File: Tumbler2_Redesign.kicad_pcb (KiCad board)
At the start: 2 copper layers, 77 x 84 mm, 4 parts

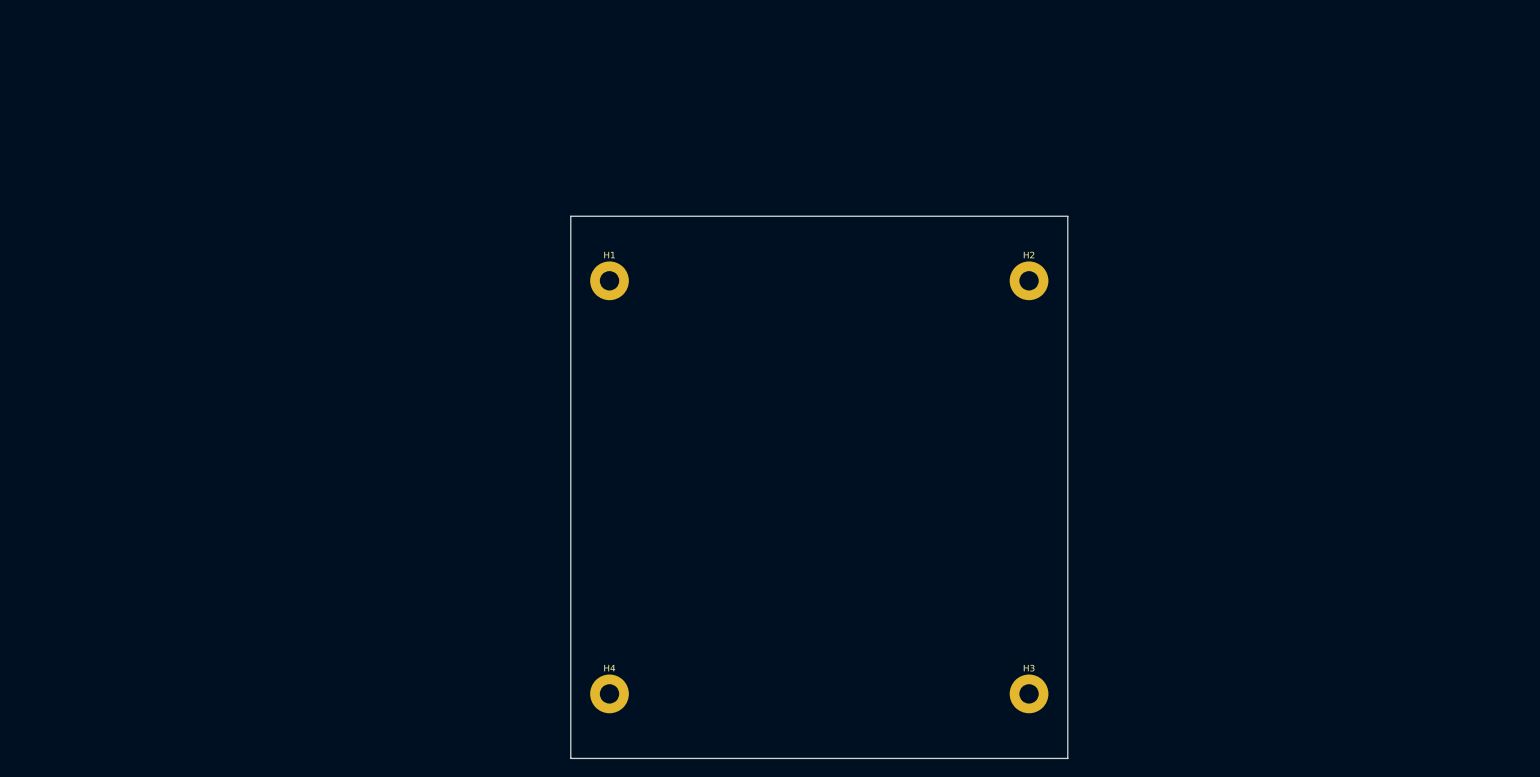
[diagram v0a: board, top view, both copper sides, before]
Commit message: Add HC-SR04 3D model
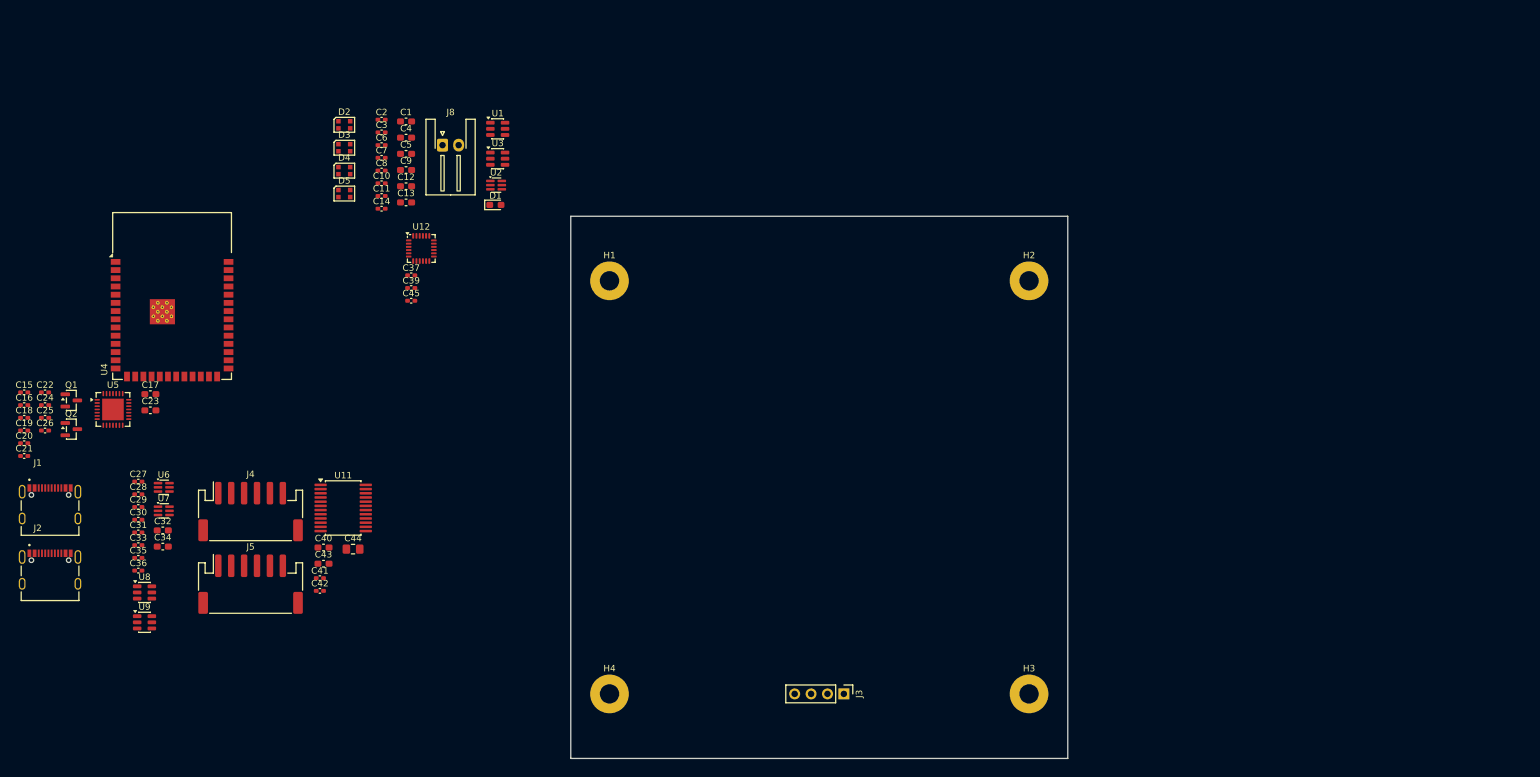
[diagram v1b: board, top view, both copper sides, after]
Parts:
- added C1: 10uF, Capacitor_SMD:C_0603_1608Metric_Pad1.08x0.95mm_HandSolder, F.Cu at (88.3, 46.7)
- added C10: 100nF, Capacitor_SMD:C_0402_1005Metric_Pad0.74x0.62mm_HandSolder, F.Cu at (84.5, 56.2)
- added C11: 100nF, Capacitor_SMD:C_0402_1005Metric_Pad0.74x0.62mm_HandSolder, F.Cu at (84.5, 58.2)
- added C12: 22uF, Capacitor_SMD:C_0603_1608Metric_Pad1.08x0.95mm_HandSolder, F.Cu at (88.3, 56.7)
- added C13: 22uF, Capacitor_SMD:C_0603_1608Metric_Pad1.08x0.95mm_HandSolder, F.Cu at (88.3, 59.2)
- added C14: 100nF, Capacitor_SMD:C_0402_1005Metric_Pad0.74x0.62mm_HandSolder, F.Cu at (84.5, 60.2)
- added C15: 100nF, Capacitor_SMD:C_0402_1005Metric_Pad0.74x0.62mm_HandSolder, F.Cu at (29.1, 88.7)
- added C16: 4.7uF, Capacitor_SMD:C_0402_1005Metric_Pad0.74x0.62mm_HandSolder, F.Cu at (29.1, 90.6)
- added C17: 10uF, Capacitor_SMD:C_0603_1608Metric_Pad1.08x0.95mm_HandSolder, F.Cu at (48.7, 88.9)
- added C18: 100nF, Capacitor_SMD:C_0402_1005Metric_Pad0.74x0.62mm_HandSolder, F.Cu at (29.1, 92.6)
- added C19: 100nF, Capacitor_SMD:C_0402_1005Metric_Pad0.74x0.62mm_HandSolder, F.Cu at (29.1, 94.6)
- added C2: 100nF, Capacitor_SMD:C_0402_1005Metric_Pad0.74x0.62mm_HandSolder, F.Cu at (84.5, 46.4)
- added C20: 100nF, Capacitor_SMD:C_0402_1005Metric_Pad0.74x0.62mm_HandSolder, F.Cu at (29.1, 96.5)
- added C21: 100nF, Capacitor_SMD:C_0402_1005Metric_Pad0.74x0.62mm_HandSolder, F.Cu at (29.1, 98.5)
- added C22: 100nF, Capacitor_SMD:C_0402_1005Metric_Pad0.74x0.62mm_HandSolder, F.Cu at (32.4, 88.7)
- added C23: 10uF, Capacitor_SMD:C_0603_1608Metric_Pad1.08x0.95mm_HandSolder, F.Cu at (48.7, 91.4)
- added C24: 100nF, Capacitor_SMD:C_0402_1005Metric_Pad0.74x0.62mm_HandSolder, F.Cu at (32.4, 90.6)
- added C25: 100nF, Capacitor_SMD:C_0402_1005Metric_Pad0.74x0.62mm_HandSolder, F.Cu at (32.4, 92.6)
- added C26: 100nF, Capacitor_SMD:C_0402_1005Metric_Pad0.74x0.62mm_HandSolder, F.Cu at (32.4, 94.6)
- added C27: 100nF, Capacitor_SMD:C_0402_1005Metric_Pad0.74x0.62mm_HandSolder, F.Cu at (46.8, 102.5)
- added C28: 100nF, Capacitor_SMD:C_0402_1005Metric_Pad0.74x0.62mm_HandSolder, F.Cu at (46.8, 104.4)
- added C29: 100nF, Capacitor_SMD:C_0402_1005Metric_Pad0.74x0.62mm_HandSolder, F.Cu at (46.8, 106.4)
- added C3: 100nF, Capacitor_SMD:C_0402_1005Metric_Pad0.74x0.62mm_HandSolder, F.Cu at (84.5, 48.4)
- added C30: 100nF, Capacitor_SMD:C_0402_1005Metric_Pad0.74x0.62mm_HandSolder, F.Cu at (46.8, 108.4)
- added C31: 100nF, Capacitor_SMD:C_0402_1005Metric_Pad0.74x0.62mm_HandSolder, F.Cu at (46.8, 110.3)
- added C32: 10uF, Capacitor_SMD:C_0603_1608Metric_Pad1.08x0.95mm_HandSolder, F.Cu at (50.6, 110.0)
- added C33: 100nF, Capacitor_SMD:C_0402_1005Metric_Pad0.74x0.62mm_HandSolder, F.Cu at (46.8, 112.3)
- added C34: 10uF, Capacitor_SMD:C_0603_1608Metric_Pad1.08x0.95mm_HandSolder, F.Cu at (50.6, 112.5)
- added C35: 100nF, Capacitor_SMD:C_0402_1005Metric_Pad0.74x0.62mm_HandSolder, F.Cu at (46.8, 114.3)
- added C36: 100nF, Capacitor_SMD:C_0402_1005Metric_Pad0.74x0.62mm_HandSolder, F.Cu at (46.8, 116.3)
- added C37: 100nF, Capacitor_SMD:C_0402_1005Metric_Pad0.74x0.62mm_HandSolder, F.Cu at (89.1, 70.5)
- added C39: 2.2nF, Capacitor_SMD:C_0402_1005Metric_Pad0.74x0.62mm_HandSolder, F.Cu at (89.1, 72.5)
- added C4: 22uF, Capacitor_SMD:C_0603_1608Metric_Pad1.08x0.95mm_HandSolder, F.Cu at (88.3, 49.2)
- added C40: 10uF, Capacitor_SMD:C_0603_1608Metric_Pad1.08x0.95mm_HandSolder, F.Cu at (75.5, 112.7)
- added C41: 100nF, Capacitor_SMD:C_0402_1005Metric_Pad0.74x0.62mm_HandSolder, F.Cu at (74.9, 117.4)
- added C42: 100nF, Capacitor_SMD:C_0402_1005Metric_Pad0.74x0.62mm_HandSolder, F.Cu at (74.9, 119.4)
- added C43: 10uF, Capacitor_SMD:C_0603_1608Metric_Pad1.08x0.95mm_HandSolder, F.Cu at (75.5, 115.2)
- added C44: 670uF, Capacitor_SMD:C_0805_2012Metric_Pad1.18x1.45mm_HandSolder, F.Cu at (80.1, 112.9)
- added C45: 100nF, Capacitor_SMD:C_0402_1005Metric_Pad0.74x0.62mm_HandSolder, F.Cu at (89.1, 74.5)
- added C5: 22uF, Capacitor_SMD:C_0603_1608Metric_Pad1.08x0.95mm_HandSolder, F.Cu at (88.3, 51.7)
- added C6: 100nF, Capacitor_SMD:C_0402_1005Metric_Pad0.74x0.62mm_HandSolder, F.Cu at (84.5, 50.3)
- added C7: 100nF, Capacitor_SMD:C_0402_1005Metric_Pad0.74x0.62mm_HandSolder, F.Cu at (84.5, 52.3)
- added C8: 100nF, Capacitor_SMD:C_0402_1005Metric_Pad0.74x0.62mm_HandSolder, F.Cu at (84.5, 54.3)
- added C9: 10uF, Capacitor_SMD:C_0603_1608Metric_Pad1.08x0.95mm_HandSolder, F.Cu at (88.3, 54.2)
- added D1: LED, LED_SMD:LED_0603_1608Metric_Pad1.05x0.95mm_HandSolder, F.Cu at (102.1, 59.6)
- added D2: WS2812B, LED_SMD:LED_WS2812B-2020_PLCC4_2.0x2.0mm, F.Cu at (78.7, 47.2)
- added D3: WS2812B, LED_SMD:LED_WS2812B-2020_PLCC4_2.0x2.0mm, F.Cu at (78.7, 50.7)
- added D4: WS2812B, LED_SMD:LED_WS2812B-2020_PLCC4_2.0x2.0mm, F.Cu at (78.7, 54.3)
- added D5: WS2812B, LED_SMD:LED_WS2812B-2020_PLCC4_2.0x2.0mm, F.Cu at (78.7, 57.8)
- added J1: USB_C_Receptacle_USB2.0_16P, Tumbler2:KINGHELM_KH-TYPE-C-16P, F.Cu at (33.1, 108.2)
- added J2: USB_C_Receptacle_USB2.0_16P, Tumbler2:KINGHELM_KH-TYPE-C-16P, F.Cu at (33.1, 118.3)
- added J3: Conn_01x04, Connector_PinHeader_2.54mm:PinHeader_1x04_P2.54mm_Vertical, F.Cu at (156.1, 135.4)
- added J4: Conn_01x06, Connector_JST:JST_PH_S6B-PH-SM4-TB_1x06-1MP_P2.00mm_Horizontal, F.Cu at (64.2, 107.1)
- added J5: Conn_01x06, Connector_JST:JST_PH_S6B-PH-SM4-TB_1x06-1MP_P2.00mm_Horizontal, F.Cu at (64.2, 118.4)
- added J8: Conn_01x02, Connector_JST:JST_XH_S2B-XH-A-1_1x02_P2.50mm_Horizontal, F.Cu at (93.9, 50.3)
- added Q1: BC817, Package_TO_SOT_SMD:SOT-23, F.Cu at (36.4, 89.9)
- added Q2: BC817, Package_TO_SOT_SMD:SOT-23, F.Cu at (36.4, 94.3)
- added U1: AP63205WU, Package_TO_SOT_SMD:TSOT-23-6, F.Cu at (102.5, 47.8)
- added U11: TB6612FNG, Package_SO:SSOP-24_5.3x8.2mm_P0.65mm, F.Cu at (78.5, 106.6)
- added U12: MPU-6050, Sensor_Motion:InvenSense_QFN-24_4x4mm_P0.5mm, F.Cu at (90.6, 66.3)
- added U2: LM66100DCK, Package_TO_SOT_SMD:SOT-363_SC-70-6, F.Cu at (102.2, 56.5)
- added U3: AP63203WU, Package_TO_SOT_SMD:TSOT-23-6, F.Cu at (102.5, 52.4)
- added U4: ESP32-S3-WROOM-1, RF_Module:ESP32-S3-WROOM-1, F.Cu at (52.0, 73.7)
- added U5: CP2102N-A02-GQFN28R, Package_DFN_QFN:QFN-28-1EP_5x5mm_P0.5mm_EP3.35x3.35mm, F.Cu at (42.9, 91.3)
- added U6: LM66100DCK, Package_TO_SOT_SMD:SOT-363_SC-70-6, F.Cu at (50.7, 103.4)
- added U7: LM66100DCK, Package_TO_SOT_SMD:SOT-363_SC-70-6, F.Cu at (50.7, 107.0)
- added U8: USBLC6-2SC6, Package_TO_SOT_SMD:SOT-23-6, F.Cu at (47.8, 119.6)
- added U9: USBLC6-2SC6, Package_TO_SOT_SMD:SOT-23-6, F.Cu at (47.8, 124.3)

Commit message: Correct pin header rotation
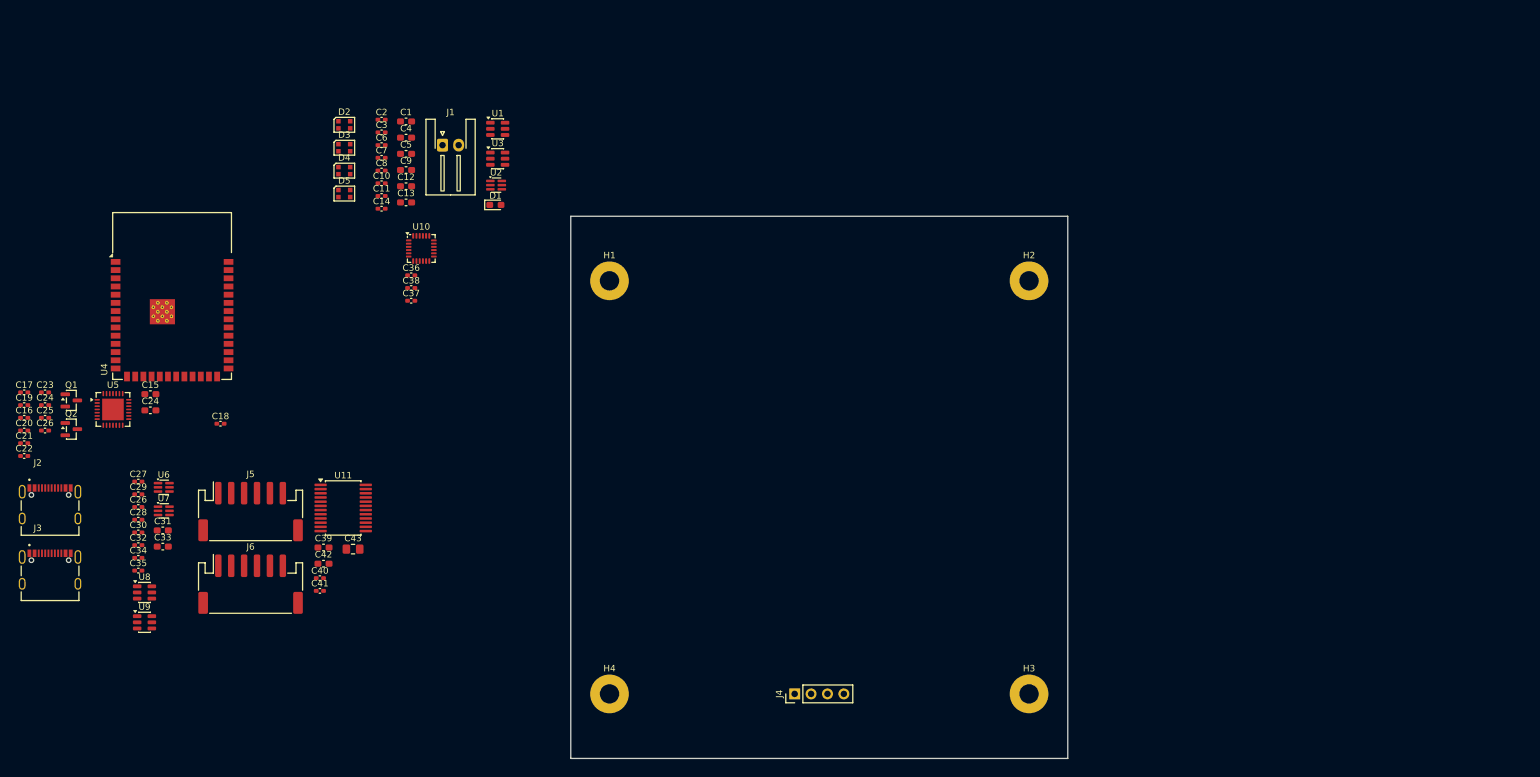
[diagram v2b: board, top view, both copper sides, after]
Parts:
- added C18: 100nF, Capacitor_SMD:C_0402_1005Metric_Pad0.74x0.62mm_HandSolder, F.Cu at (59.5, 93.5)
- C19: renamed from C16; value 4.7uF -> 10uF
- C25: value 100nF -> 1uF
- moved J4 7.62 mm to (148.5, 135.4), turned to 90 degrees
- renumbered C17 to C15, C18 to C16, C15 to C17, C19 to C20, C20 to C21, C21 to C22, C22 to C23, C23 to C24, C29 to C26, C30 to C28, C28 to C29, C31 to C30, C32 to C31, C33 to C32, C34 to C33, C35 to C34, C36 to C35, C37 to C36, C45 to C37, C39 to C38, C40 to C39, C41 to C40, C42 to C41, C43 to C42, C44 to C43, J8 to J1, J1 to J2, J2 to J3, J3 to J4, J4 to J5, J5 to J6, U12 to U10
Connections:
- U10 pad 23: /Sensors/SCL -> /MCU/SCL
- U10 pad 24: /Sensors/SDA -> /MCU/SDA
- U5 pad 9: 3.3V -> Net-(U5-~{RST})

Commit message: Add expansion pin headers
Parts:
- added U12: MCP23S17_SS, Package_SO:SSOP-28_5.3x10.2mm_P0.65mm, F.Cu at (82.7, 130.7)
- turned J6 to 90 degrees

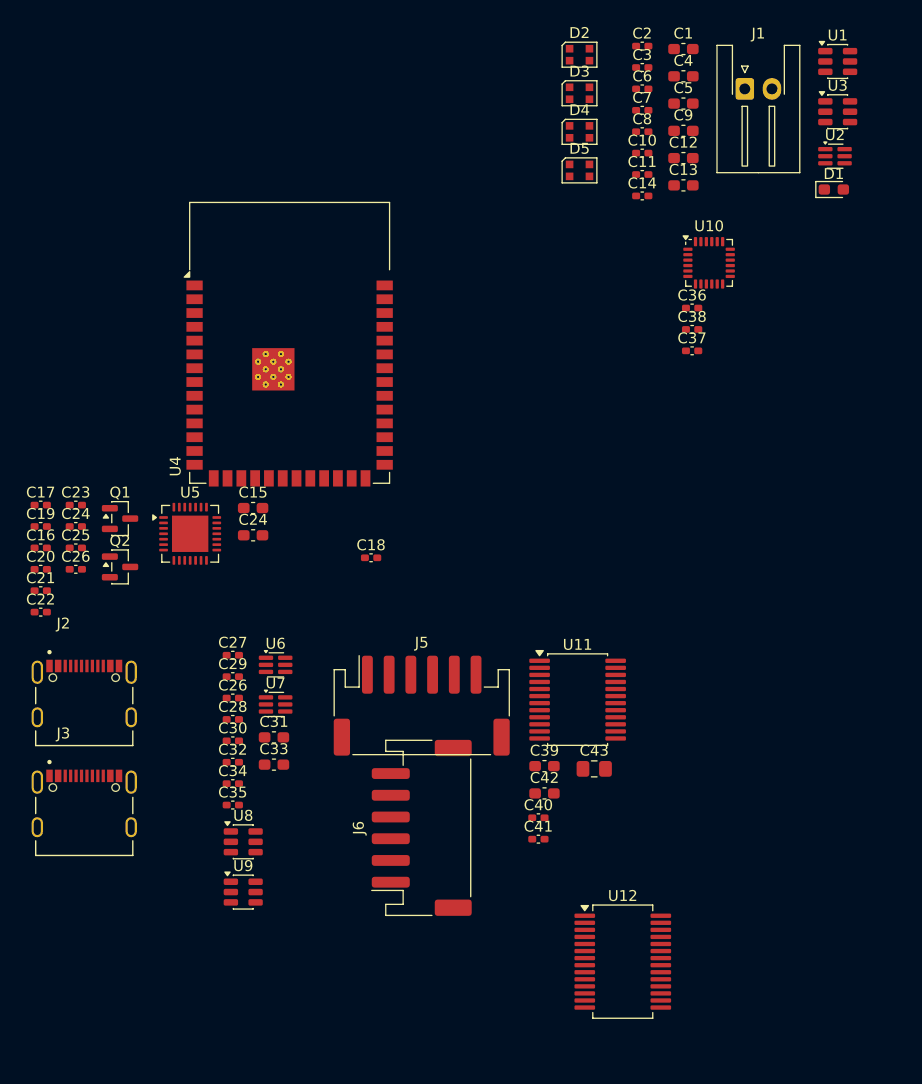
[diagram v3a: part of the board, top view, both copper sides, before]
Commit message: Correct voltage level translation
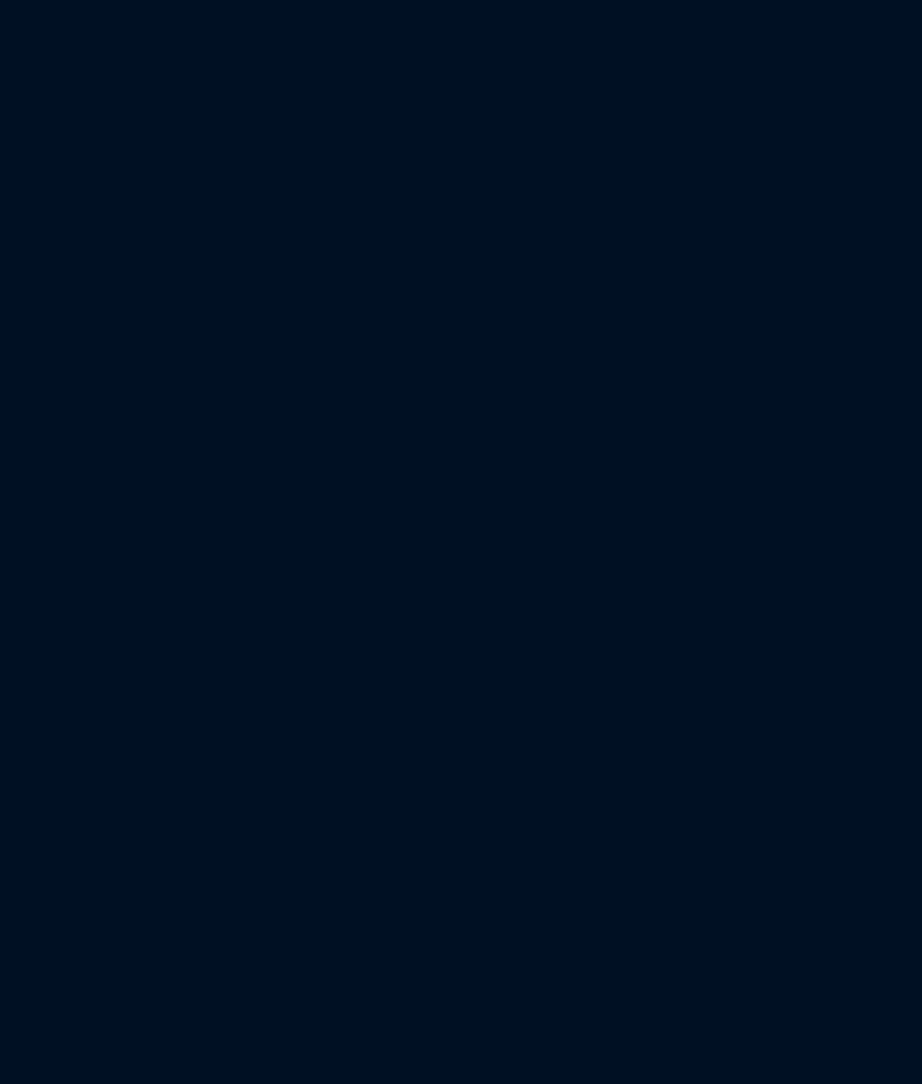
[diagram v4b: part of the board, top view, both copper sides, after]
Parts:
- removed C1, C15, C24, C31, C33, C39, C42, C9: 10uF, Capacitor_SMD:C_0603_1608Metric_Pad1.08x0.95mm_HandSolder
- removed C10, C11, C14, C16, C17, C18, C2, C20, C21, C22, C23, C24, C26 (x2), C27, C28, C29, C3, C30, C32, C34, C35, C36, C37, C40, C41, C6, C7, C8: 100nF, Capacitor_SMD:C_0402_1005Metric_Pad0.74x0.62mm_HandSolder
- removed C12, C13, C4, C5: 22uF, Capacitor_SMD:C_0603_1608Metric_Pad1.08x0.95mm_HandSolder
- removed C19: 10uF, Capacitor_SMD:C_0402_1005Metric_Pad0.74x0.62mm_HandSolder
- removed C25: 1uF, Capacitor_SMD:C_0402_1005Metric_Pad0.74x0.62mm_HandSolder
- removed C38: 2.2nF, Capacitor_SMD:C_0402_1005Metric_Pad0.74x0.62mm_HandSolder
- removed C43: 670uF, Capacitor_SMD:C_0805_2012Metric_Pad1.18x1.45mm_HandSolder
- removed D1: LED, LED_SMD:LED_0603_1608Metric_Pad1.05x0.95mm_HandSolder
- removed D2, D3, D4, D5: WS2812B, LED_SMD:LED_WS2812B-2020_PLCC4_2.0x2.0mm
- removed J1: Conn_01x02, Connector_JST:JST_XH_S2B-XH-A-1_1x02_P2.50mm_Horizontal
- removed J2, J3: USB_C_Receptacle_USB2.0_16P, Tumbler2:KINGHELM_KH-TYPE-C-16P
- removed J5, J6: Conn_01x06, Connector_JST:JST_PH_S6B-PH-SM4-TB_1x06-1MP_P2.00mm_Horizontal
- removed Q1, Q2: BC817, Package_TO_SOT_SMD:SOT-23
- removed U1: AP63205WU, Package_TO_SOT_SMD:TSOT-23-6
- removed U10: MPU-6050, Sensor_Motion:InvenSense_QFN-24_4x4mm_P0.5mm
- removed U11: TB6612FNG, Package_SO:SSOP-24_5.3x8.2mm_P0.65mm
- removed U12: MCP23S17_SS, Package_SO:SSOP-28_5.3x10.2mm_P0.65mm
- removed U2, U6, U7: LM66100DCK, Package_TO_SOT_SMD:SOT-363_SC-70-6
- removed U3: AP63203WU, Package_TO_SOT_SMD:TSOT-23-6
- removed U4: ESP32-S3-WROOM-1, RF_Module:ESP32-S3-WROOM-1
- removed U5: CP2102N-A02-GQFN28R, Package_DFN_QFN:QFN-28-1EP_5x5mm_P0.5mm_EP3.35x3.35mm
- removed U8, U9: USBLC6-2SC6, Package_TO_SOT_SMD:SOT-23-6

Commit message: Assign footprints and parts
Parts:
- removed J4: Conn_01x04, Connector_PinHeader_2.54mm:PinHeader_1x04_P2.54mm_Vertical
